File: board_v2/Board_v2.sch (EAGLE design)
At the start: 42 parts, among them IC1 MAX7219, IC2 MAX7219, IC3 MAX7219, SW1 ROTARY SWITCH, SW2 ROTARY SWITCH

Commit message: more pull down updates
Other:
- moved on the sheet: BTN, C3, C4, IC2, R2, R5

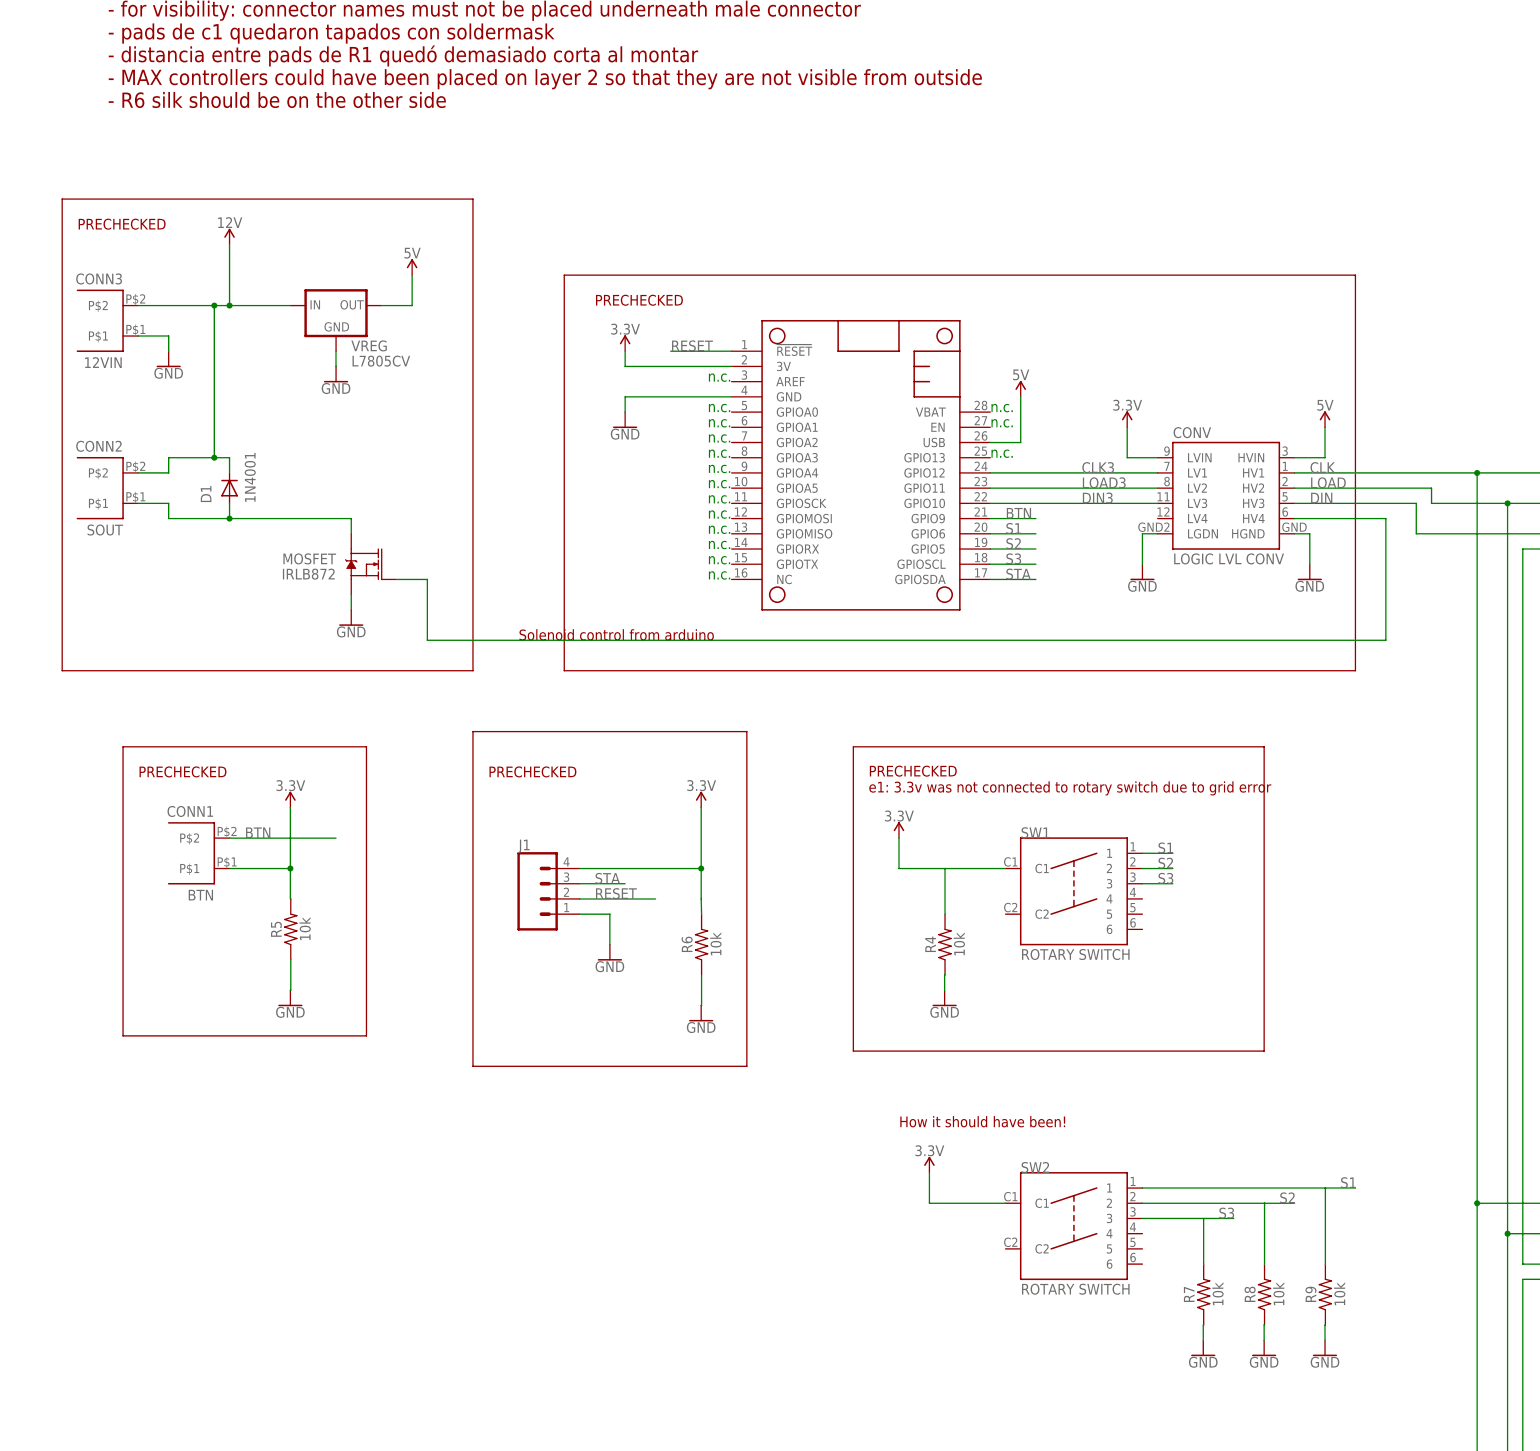
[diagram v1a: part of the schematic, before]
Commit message: new annotations to boardv2 files
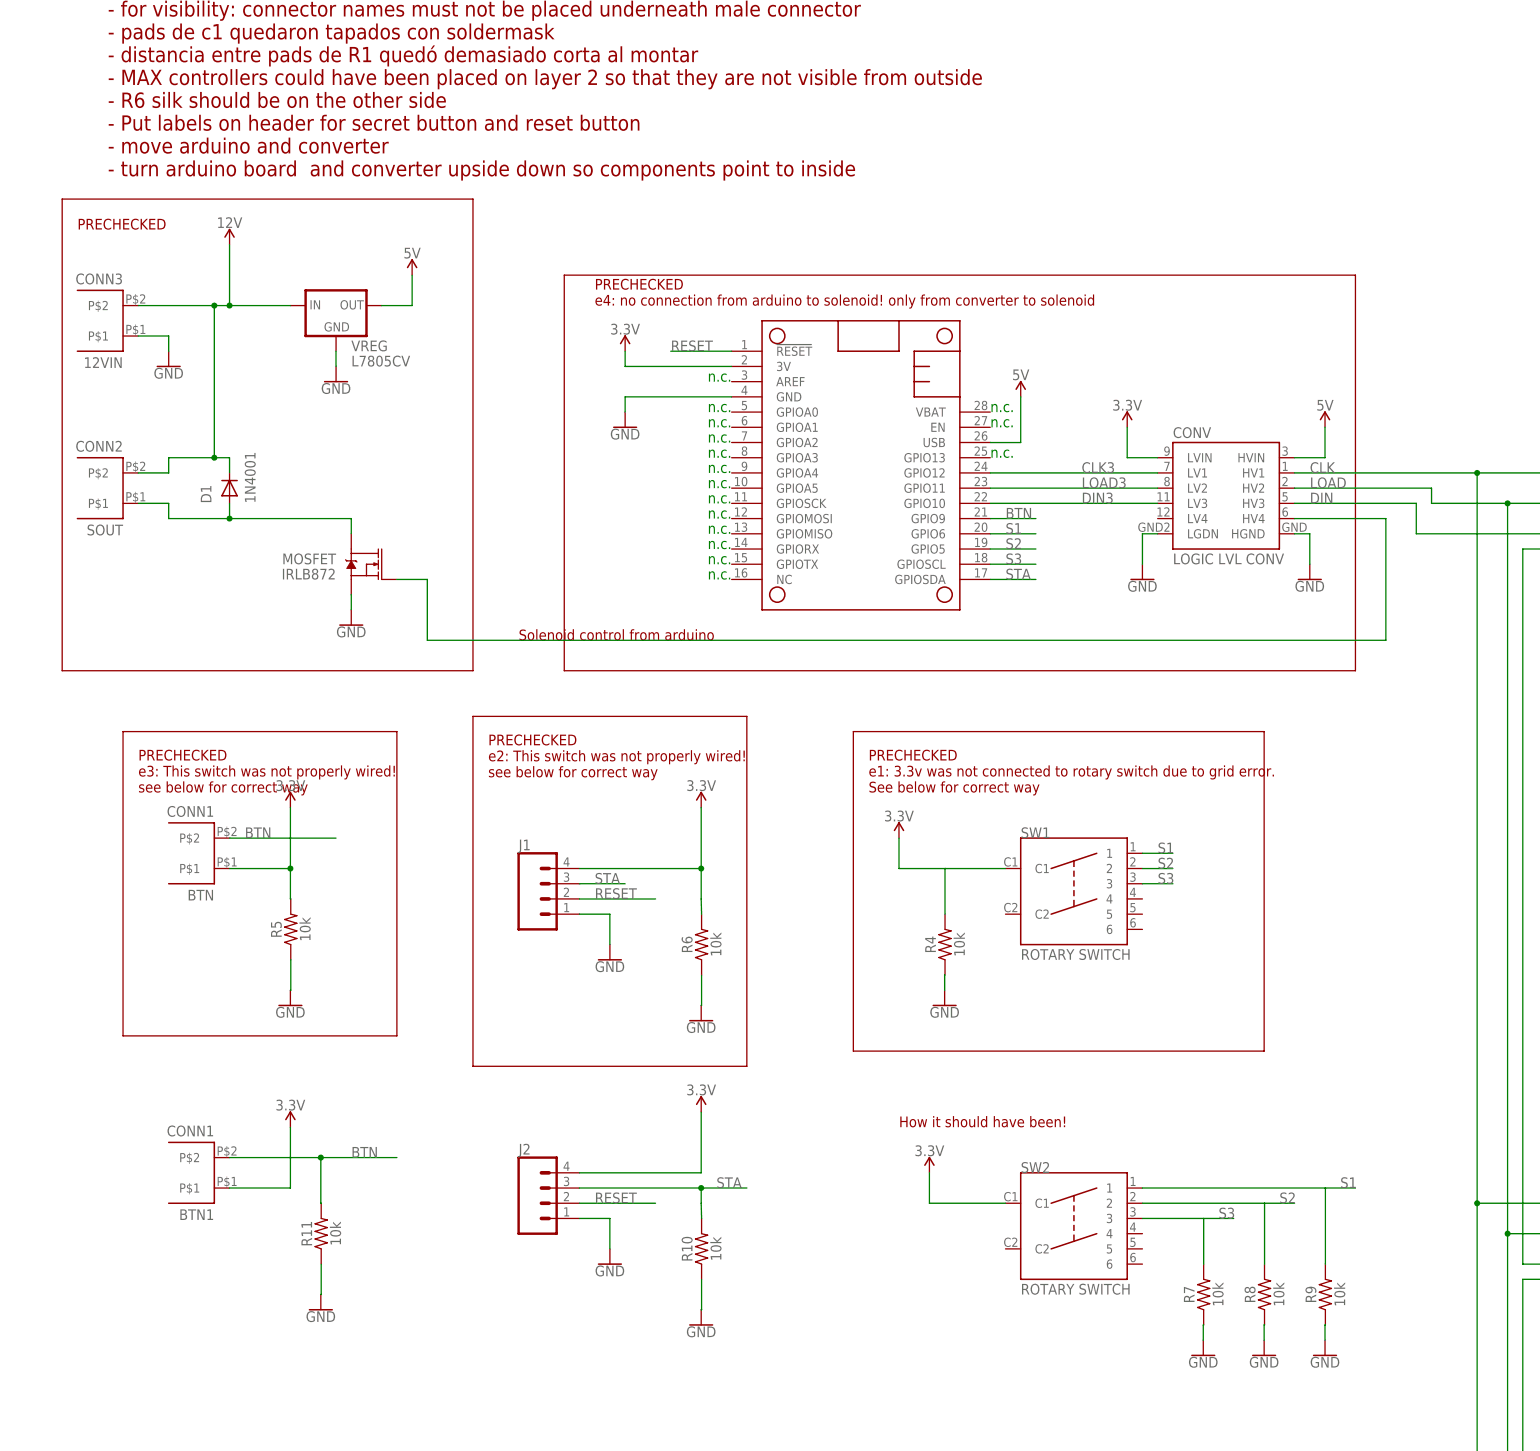
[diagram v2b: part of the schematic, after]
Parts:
- added BTN1: CONN1, AES_lib:MICRO-FIT_3.0_43650
- added J2: (no value), SparkFun-Connectors:CONN_041X04_NO_SILK
- added R10, R11: 10k, AES_lib:RESISTOR
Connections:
- net 3.3V: now also BTN1.P$1, J2.4
- net BTN: now also BTN1.P$2, R11.2
- net GND: now also J2.1, R10.1, R11.1
- net RESET: now also J2.2
- net STA: now also J2.3, R10.2
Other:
- note added: "PRECHECKED e1: 3.3v was not connected to rotary switch due to grid error. See below for correct way"
- note added: "PRECHECKED e2: This switch was not properly wired! see below for correct way"
- note added: "PRECHECKED e3: This switch was not properly wired! see below for correct way"
- note added: "PRECHECKED e4: no connection from arduino to solenoid! only from converter to solenoid"
- note removed: "PRECHECKED e1: 3.3v was not connected to rotary switch due to grid error"

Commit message: boardv2 files annotated with new found errors
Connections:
- new net N$10: SEV8.7DP
- new net N$11: SEV10.7DP
- new net N$12: SEV5.7DP
- new net N$4: SEV4.7DP
- new net N$5: SEV3.7DP
- new net N$6: SEV2.7DP
- new net N$7: SEV1.7DP
- new net SOL: CONV.LV4, FEATHERM0.GPIOA0
- net SEGDP1: no longer IC1.SEGDP
- net SEGDP2: no longer IC2.SEGDP
- net SEGDP3: no longer IC3.SEGDP
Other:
- note added: "PRECHECKED e4: no connection from arduino to solenoid! only from converter to solenoid. A0 - A5 can be used for this"
- note added: "This net was not on board v1"
- note removed: "PRECHECKED e4: no connection from arduino to solenoid! only from converter to solenoid"
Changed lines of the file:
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@@
 <text x="-439.42" y="467.36" size="1.778" layer="91">n.c.</text>
 <text x="-482.6" y="480.06" size="1.778" layer="91" rot="MR0">n.c.</text>
-<text x="-482.6" y="474.98" size="1.778" layer="91" rot="MR0">n.c.</text>
 <text x="-482.6" y="472.44" size="1.778" layer="91" rot="MR0">n.c.</text>
 <text x="-482.6" y="469.9" size="1.778" layer="91" rot="MR0">n.c.</text>
@@
 <text x="-482.6" y="449.58" size="1.778" layer="91" rot="MR0">n.c.</text>
 <text x="-482.6" y="447.04" size="1.778" layer="91" rot="MR0">n.c.</text>
-<wire x1="2.54" y1="-2.54" x2="2.54" y2="591.82" width="0.1524" layer="94"/>
-<wire x1="2.54" y1="591.82" x2="-612.14" y2="591.82" width="0.1524" layer="94"/>
-<wire x1="-612.14" y1="591.82" x2="-612.14" y2="-2.54" width="0.1524" layer="94"/>
+<wire x1="2.54" y1="-2.54" x2="2.54" y2="617.22" width="0.1524" layer="94"/>
+<wire x1="2.54" y1="617.22" x2="-612.14" y2="617.22" width="0.1524" layer="94"/>
+<wire x1="-612.14" y1="617.22" x2="-612.14" y2="-2.54" width="0.1524" layer="94"/>
 <wire x1="-612.14" y1="-2.54" x2="2.54" y2="-2.54" width="0.1524" layer="94"/>
 <wire x1="-137.16" y1="86.36" x2="-210.82" y2="86.36" width="0.1524" layer="94"/>
@@
 <wire x1="-393.7" y1="368.3" x2="-462.28" y2="368.3" width="0.1524" layer="94"/>
 <wire x1="-462.28" y1="368.3" x2="-462.28" y2="421.64" width="0.1524" layer="94"/>
-<text x="-586.74" y="574.04" size="2.54" layer="94" align="top-left">Board  v1: with review annotations
+<text x="-589.28" y="601.98" size="2.54" layer="94" align="top-left">Board  v1: with review annotations
 - convert holes to components
 - debounce buttons
@@
 - Put labels on header for secret button and reset button
 - move arduino and converter
-- turn arduino board  and converter upside down so components point to inside</text>
+- turn arduino board  and converter upside down so components point to inside
+- remove al DP connections to seven segments!
+- fix grid error on symbols</text>
 <wire x1="-480.06" y1="424.18" x2="-480.06" y2="365.76" width="0.1524" layer="94"/>
 <wire x1="-480.06" y1="365.76" x2="-525.78" y2="365.76" width="0.1524" layer="94"/>
@@
 <wire x1="-525.78" y1="510.54" x2="-525.78" y2="431.8" width="0.1524" layer="94"/>
 <text x="-518.16" y="436.88" size="1.778" layer="94">Solenoid control from arduino</text>
-<wire x1="-510.54" y1="497.84" x2="-510.54" y2="431.8" width="0.1524" layer="94"/>
+<wire x1="-510.54" y1="502.92" x2="-510.54" y2="431.8" width="0.1524" layer="94"/>
 <wire x1="-510.54" y1="431.8" x2="-378.46" y2="431.8" width="0.1524" layer="94"/>
-<wire x1="-378.46" y1="431.8" x2="-378.46" y2="497.84" width="0.1524" layer="94"/>
-<wire x1="-378.46" y1="497.84" x2="-510.54" y2="497.84" width="0.1524" layer="94"/>
+<wire x1="-378.46" y1="431.8" x2="-378.46" y2="502.92" width="0.1524" layer="94"/>
+<wire x1="-378.46" y1="502.92" x2="-510.54" y2="502.92" width="0.1524" layer="94"/>
 <text x="-505.46" y="492.76" size="1.778" layer="94">PRECHECKED
-e4: no connection from arduino to solenoid! only from converter to solenoid</text>
+e4: no connection from arduino to solenoid! only from converter to solenoid.
+A0 - A5 can be used for this</text>
 <text x="-454.66" y="355.6" size="1.778" layer="94">How it should have been!</text>
 <text x="-581.66" y="411.48" size="1.778" layer="94">PRECHECKED
 e3: This switch was not properly wired!
 see below for correct way</text>
+<text x="-469.9" y="439.42" size="1.778" layer="94">This net was not on board v1</text>
 </plain>
 <instances>
@@
 <label x="-157.48" y="497.84" size="1.778" layer="95" rot="R90"/>
 </segment>
-<segment>
-<pinref part="IC1" gate="G$1" pin="SEGDP"/>
-<wire x1="-243.84" y1="426.72" x2="-256.54" y2="426.72" width="0.1524" layer="91"/>
-<label x="-254" y="426.72" size="1.778" layer="95"/>
-</segment>
 </net>
 <net name="SEGG1" class="0">
@@
 <net name="SEGDP2" class="0">
 <segment>
-<pinref part="IC2" gate="G$1" pin="SEGDP"/>
-<wire x1="-256.54" y1="304.8" x2="-241.3" y2="304.8" width="0.1524" layer="91"/>
-<label x="-254" y="304.8" size="1.778" layer="95"/>
-</segment>
-<segment>
 <pinref part="BAR1" gate="G$1" pin="A8"/>
 <wire x1="-157.48" y1="330.2" x2="-157.48" y2="320.04" width="0.1524" layer="91"/>
@@
 <net name="SEGDP3" class="0">
 <segment>
-<pinref part="IC3" gate="G$1" pin="SEGDP"/>
-<wire x1="-256.54" y1="147.32" x2="-243.84" y2="147.32" width="0.1524" layer="91"/>
-<label x="-254" y="147.32" size="1.778" layer="95"/>
-</segment>
-<segment>
 <pinref part="SEV7" gate="G$1" pin="7DP"/>
 <wire x1="-157.48" y1="177.799996875" x2="-157.48" y2="177.8" width="0.1524" layer="91"/>
+<wire x1="-157.48" y1="177.799996875" x2="-144.78" y2="177.799996875" width="0.1524" layer="91"/>
+<wire x1="-144.78" y1="177.799996875" x2="-144.78" y2="177.8" width="0.1524" layer="91"/>
+<junction x="-157.48" y="177.799996875"/>
+<label x="-149.86" y="177.8" size="1.778" layer="95"/>
 </segment>
 <segment>
 <pinref part="SEV9" gate="G$1" pin="7DP"/>
 <wire x1="-157.48" y1="121.919996875" x2="-157.48" y2="121.92" width="0.1524" layer="91"/>
+<wire x1="-157.48" y1="121.919996875" x2="-142.24" y2="121.919996875" width="0.1524" layer="91"/>
+<wire x1="-142.24" y1="121.919996875" x2="-142.24" y2="119.38" width="0.1524" layer="91"/>
+<junction x="-157.48" y="121.919996875"/>
+<label x="-149.86" y="121.92" size="1.778" layer="95"/>
 </segment>
 <segment>
 <pinref part="SEV6" gate="G$1" pin="7DP"/>
 <wire x1="-157.48" y1="40.639996875" x2="-157.48" y2="40.64" width="0.1524" layer="91"/>
+<wire x1="-157.48" y1="40.639996875" x2="-144.78" y2="40.639996875" width="0.1524" layer="91"/>
+<wire x1="-144.78" y1="40.639996875" x2="-144.78" y2="38.1" width="0.1524" layer="91"/>
+<junction x="-157.48" y="40.639996875"/>
+<label x="-149.86" y="40.64" size="1.778" layer="95"/>
 </segment>
 </net>
@@
 </segment>
 </net>
+<net name="SOL" class="0">
+<segment>
+<pinref part="FEATHERM0" gate="G$1" pin="GPIOA0"/>
+<wire x1="-482.6" y1="474.98" x2="-492.76" y2="474.98" width="0.1524" layer="91"/>
+<wire x1="-492.76" y1="474.98" x2="-492.76" y2="439.42" width="0.1524" layer="91"/>
+<wire x1="-492.76" y1="439.42" x2="-419.1" y2="439.42" width="0.1524" layer="91"/>
+<wire x1="-419.1" y1="439.42" x2="-419.1" y2="457.2" width="0.1524" layer="91"/>
+<pinref part="CONV" gate="G$1" pin="LV4"/>
+<wire x1="-419.1" y1="457.2" x2="-411.48" y2="457.2" width="0.1524" layer="91"/>
+<label x="-490.22" y="474.98" size="1.778" layer="95"/>
+</segment>
+</net>
+<net name="N$4" class="0">
+<segment>
+<pinref part="SEV4" gate="G$1" pin="7DP"/>
+<wire x1="-91.4908" y1="226.043065625" x2="-76.2" y2="226.043065625" width="0.1524" layer="91"/>
+<wire x1="-76.2" y1="226.043065625" x2="-76.2" y2="226.06" width="0.1524" layer="91"/>
+<label x="-78.74" y="226.06" size="1.778" layer="95"/>
+</segment>
+</net>
+<net name="N$5" class="0">
+<segment>
+<pinref part="SEV3" gate="G$1" pin="7DP"/>
+<wire x1="-91.4908" y1="248.903065625" x2="-73.66" y2="248.903065625" width="0.1524" layer="91"/>
+<wire x1="-73.66" y1="248.903065625" x2="-73.66" y2="248.92" width="0.1524" layer="91"/>
+<label x="-78.74" y="248.92" size="1.778" layer="95"/>
+</segment>
+</net>
+<net name="N$6" class="0">
+<segment>
+<pinref part="SEV2" gate="G$1" pin="7DP"/>
+<wire x1="-91.4908" y1="271.763065625" x2="-76.2" y2="271.763065625" width="0.1524" layer="91"/>
+<wire x1="-76.2" y1="271.763065625" x2="-76.2" y2="271.78" width="0.1524" layer="91"/>
+<label x="-78.74" y="271.78" size="1.778" layer="95"/>
+</segment>
+</net>
+<net name="N$7" class="0">
+<segment>
+<pinref part="SEV1" gate="G$1" pin="7DP"/>
+<wire x1="-91.4908" y1="294.623065625" x2="-91.4908" y2="294.64" width="0.1524" layer="91"/>
+<wire x1="-91.4908" y1="294.64" x2="-76.2" y2="294.64" width="0.1524" layer="91"/>
+<label x="-78.74" y="294.64" size="1.778" layer="95"/>
+</segment>
+</net>
+<net name="N$10" class="0">
+<segment>
+<pinref part="SEV8" gate="G$1" pin="7DP"/>
+<wire x1="-157.48" y1="154.937175" x2="-144.78" y2="154.937175" width="0.1524" layer="91"/>
+<wire x1="-144.78" y1="154.937175" x2="-144.78" y2="154.94" width="0.1524" layer="91"/>
+<label x="-147.32" y="154.94" size="1.778" layer="95"/>
+</segment>
+</net>
+<net name="N$11" class="0">
+<segment>
+<pinref part="SEV10" gate="G$1" pin="7DP"/>
+<wire x1="-157.48" y1="99.057175" x2="-144.78" y2="99.057175" width="0.1524" layer="91"/>
+<wire x1="-144.78" y1="99.057175" x2="-144.78" y2="96.52" width="0.1524" layer="91"/>
+</segment>
+</net>
+<net name="N$12" class="0">
+<segment>
+<pinref part="SEV5" gate="G$1" pin="7DP"/>
+<wire x1="-157.48" y1="63.497175" x2="-142.24" y2="63.497175" width="0.1524" layer="91"/>
+<wire x1="-142.24" y1="63.497175" x2="-142.24" y2="63.5" width="0.1524" layer="91"/>
+<label x="-147.32" y="63.5" size="1.778" layer="95"/>
+</segment>
+</net>
